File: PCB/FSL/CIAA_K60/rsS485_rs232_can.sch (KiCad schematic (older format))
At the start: 50 parts, among them J401 RS485, J402 DB9, J403 CAN, U401 MAX3072, U402 ST3232E, U403 TJA1040

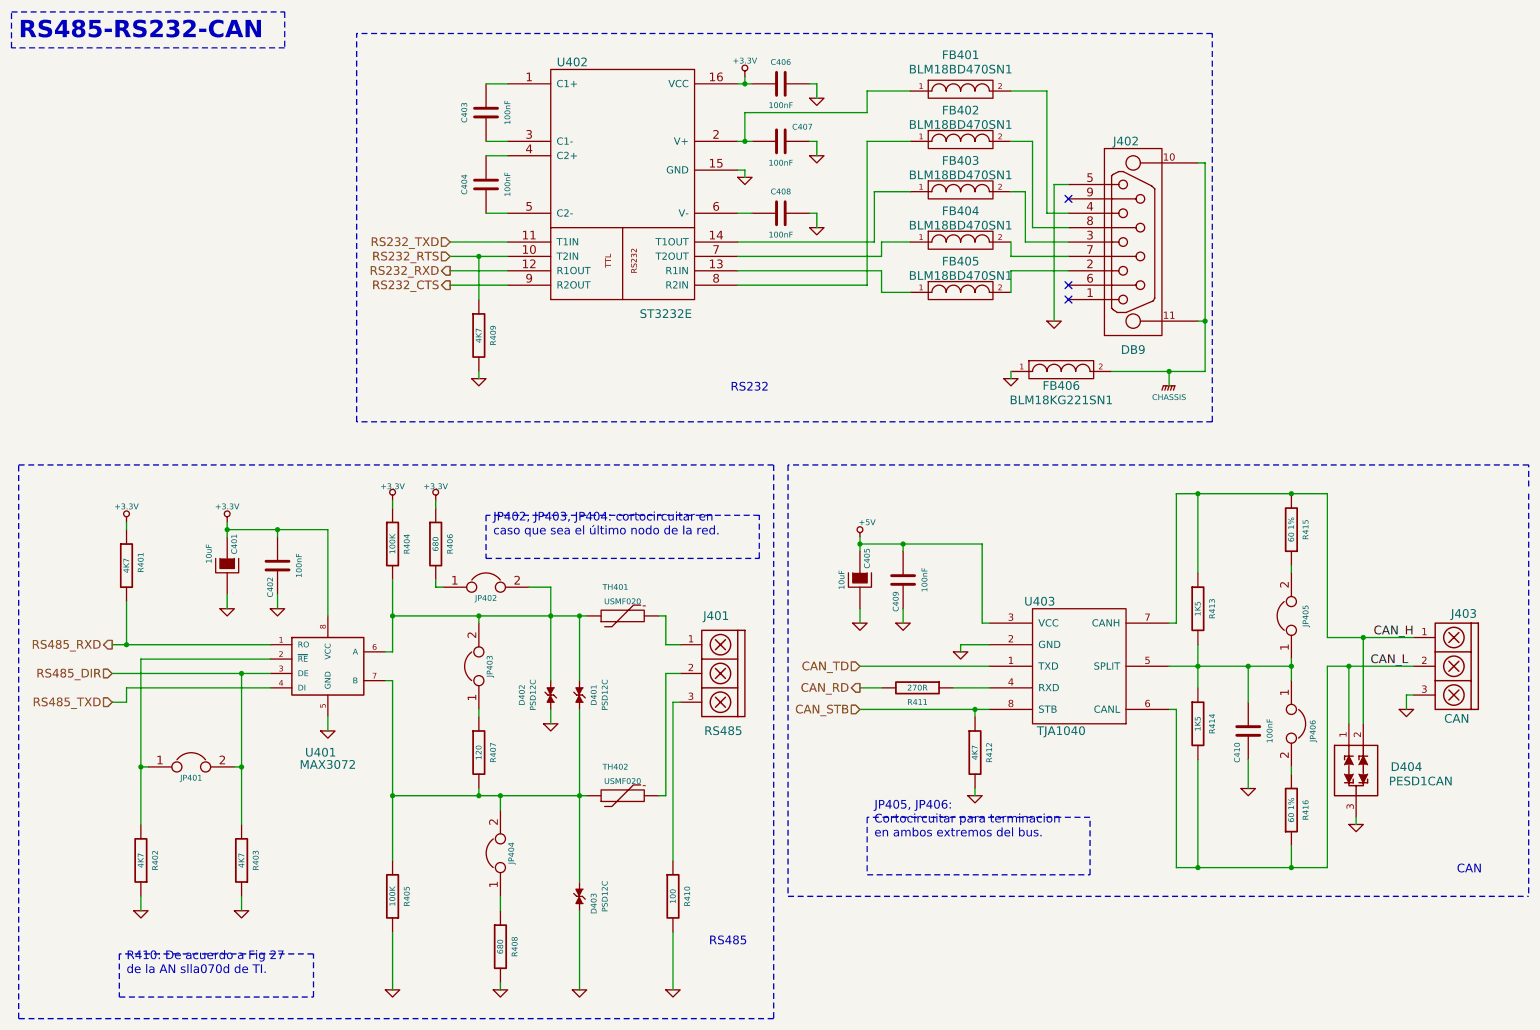
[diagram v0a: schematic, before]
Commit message: Actualizacion de esquematicos. Circuito impreso y modelos 3D
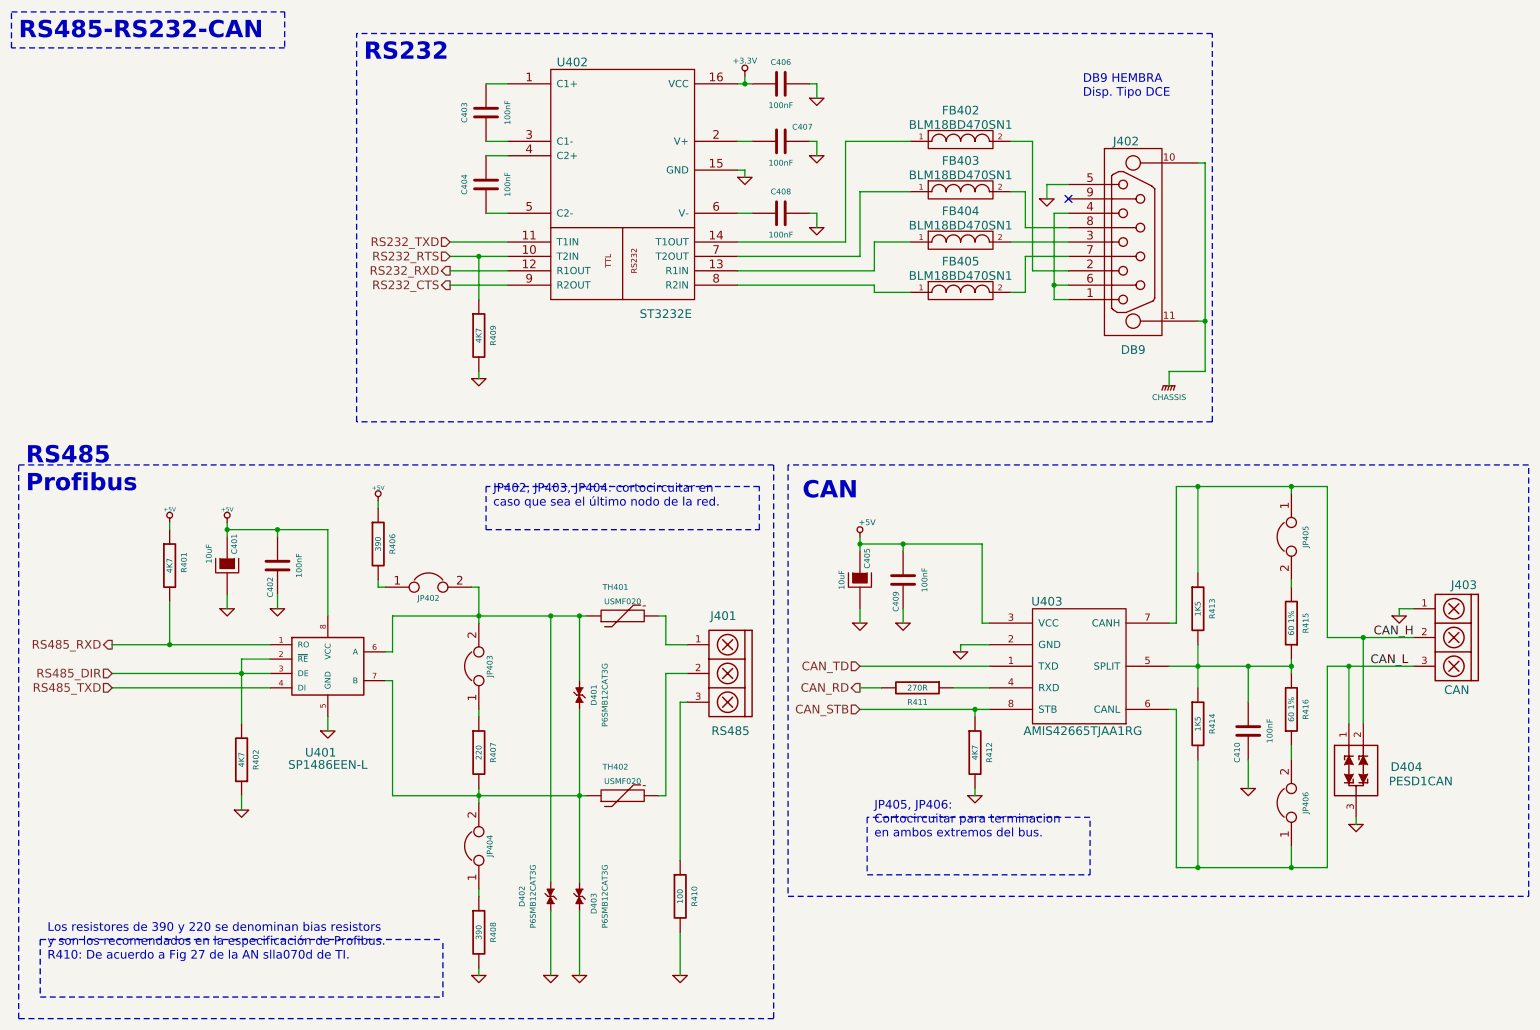
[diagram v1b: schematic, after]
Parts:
- removed FB401: BLM18BD470SN1, fb_0603, symbol FILTER
- removed FB406: BLM18KG221SN1, fb_0603, symbol FILTER
- removed JP401: JUMPER, PIN_ARRAY_2x1, symbol JUMPER
- removed R403: 4K7, r_0603, symbol R
- removed R404, R405: 100K, r_0603, symbol R
- D401, D402, D403: value PSD12C -> P6SMB12CAT3G
- J402: footprint DB9FC -> DB9_F_TH; Descripcion CONN DB9 FEMALE R/A SOLDER SMD -> CONN D-SUB RCPT 9POS RA GOLD; Digikey/Mouser 190-09FA-ND -> S9554-ND; Fabricante Norcomp Inc. -> Sullins; Footprint estandar (none) -> DB9F 7.2mm; Nro. parte 190-009-263R001 -> SDS107-PRP1-F09-SN63-11; Path datasheet ../datasheet/connectors/190-009-263R001.pdf -> ../datasheets/connectors/SDS107-PRP1-F09-SN63-11.pdf
- R406, R408: value 680 -> 390; Descripcion RES 680 OHM 1/10W 5% 0603 SMD -> RES 390 OHM 1/10W 5% 0603 SMD; Digikey/Mouser 311-680GRCT-ND -> 311-390GRCT-ND; Nro. parte RC0603JR-07680RL -> RC0603JR-07390RL
- R407: value 120 -> 220; Descripcion RES 120 OHM 1/10W 5% 0603 SMD -> RES 220 OHM 1/10W 5% 0603 SMD; Digikey/Mouser 311-120GRCT-ND -> 311-220GRCT-ND; Nro. parte RC0603JR-07120RL -> RC0603JR-07220RL
- U401: value MAX3072 -> SP1486EEN-L; Descripcion IC TXRX RS485/422 8-SOIC -> IC TXRX RS485/422 PROFIBUS 8SOIC; Digikey/Mouser MAX3072EESA+-ND -> 1016-1003-5-ND; Fabricante Maxim Integrated -> Exar Corporation; Footprint estandar 8-SOIC (0.154\", 3.90mm Width) -> SOIC-8; Nro. parte MAX3072EESA+ -> SP1486EEN-L; Path datasheet ../datasheet/ic/MAX3070E-MAX3079E.pdf -> ../datasheets/ic/SP1486EEN-L.pdf
- U403: value TJA1040 -> AMIS42665TJAA1RG; Path datasheet ../datasheet/ic/tja1040.pdf -> ../datasheets/ic/AMIS-42665-D.PDF
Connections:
- net +3.3V: no longer C401.1, C402.2, R401.1, R406.1, U401.8 (VCC)
- net +5V: now also C401.1, C402.2, R401.1, R406.1, U401.8 (VCC)
- net CAN_H: now also J403.2, JP405.1; no longer J403.1, R415.2
- net CAN_L: now also J403.3, JP406.1; no longer J403.2, R416.1
- net GND: now also J403.1; no longer J403.3
- net RS485_DIR: now also R402.2, U401.2 (~RE~)
- net at J402.1 (Data_Carrier_Detect): now also J402.4 (DTR), J402.6 (DSR)
- net at J402.2 (Receive_Data): now also FB402.2; no longer FB405.2
- net at J402.3 (Transmit_Data): now also FB404.2; no longer FB403.2
- net at J402.7 (RTS): now also FB405.2; no longer FB404.2
- net at J402.8 (CTS): now also FB403.2; no longer FB402.2
- net at C410.1, R413.2, R414.1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: now also R415.1, R416.2; no longer JP405.1, JP406.1
- net at JP405.2: now also R415.2; no longer R415.1
- net at JP406.2: now also R416.1; no longer R416.2
- net at U402.13 (R1IN): now also FB404.1; no longer FB405.1
- net at U402.14 (T1OUT): now also FB402.1; no longer FB403.1
- net at U402.7 (T2OUT): now also FB403.1; no longer FB404.1
- net at U402.8 (R2IN): now also FB405.1; no longer FB402.1
- no-connect marks 3 -> 1
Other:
- note added: "DB9 HEMBRA\nDisp. Tipo DCE"
- note added: "Los resistores de 390 y 220 se denominan bias resistors\ny son los recomendados en la especificación de Profibus.\nR410: De acuerdo a Fig 27 de la AN slla070d de TI."
- note added: "RS485\nProfibus"
- note removed: "R410: De acuerdo a Fig 27 \nde la AN slla070d de TI.\n"
- note removed: "RS485"
- moved on the sheet: D402, J401, J403, JP402, JP404, JP405, JP406, R401, R402, R406, R410, R415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

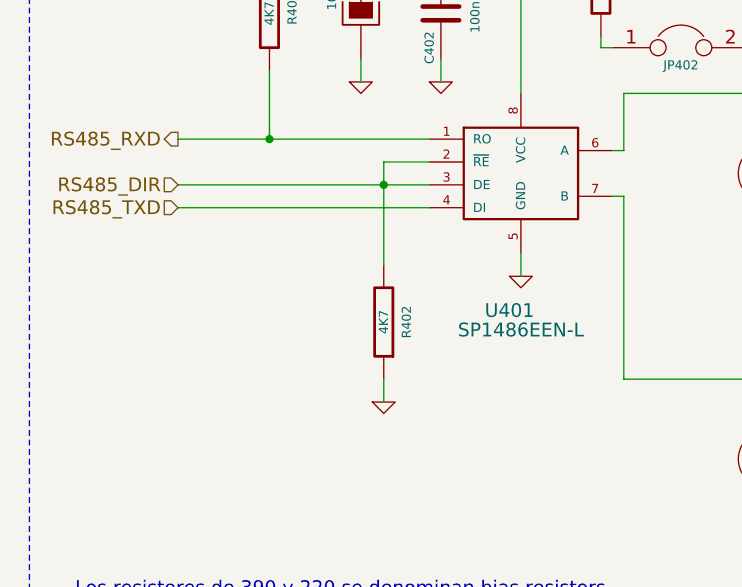
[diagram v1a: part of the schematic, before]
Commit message: - Actualizado PCB - Actualizado documentación - Agregado scripts complementarios de kicad.
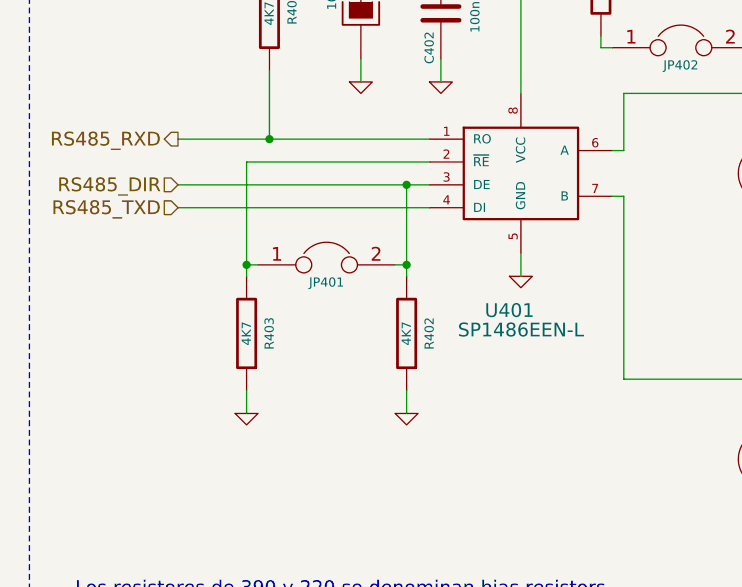
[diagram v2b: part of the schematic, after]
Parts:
- added JP401: JUMPER, PIN_ARRAY_2x1, symbol JUMPER
- added R403: 4K7, r_0603, symbol R
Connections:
- net GND: now also R403.1
- net RS485_DIR: now also JP401.2; no longer U401.2 (~RE~)
- new net: JP401.1, R403.2, U401.2 (~RE~)
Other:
- moved on the sheet: R402

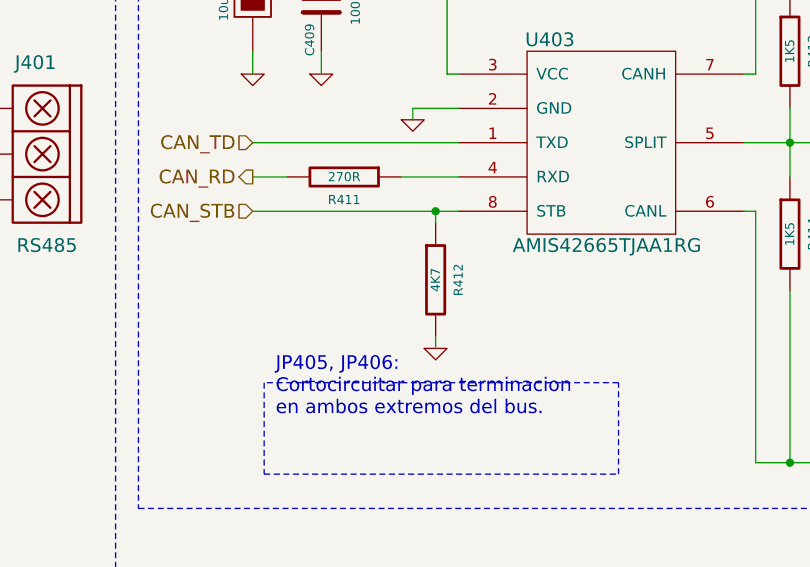
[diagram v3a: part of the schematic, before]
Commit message: CIAA-FSL Versión CEIBO 1.1 - Resumen de cambios en FSL/CIAA_K60/doc/modificaciones - Agregado info de puesta en marcha CEIBO 1.0 - Agregado info de fabricación de la CEIBO 1.0
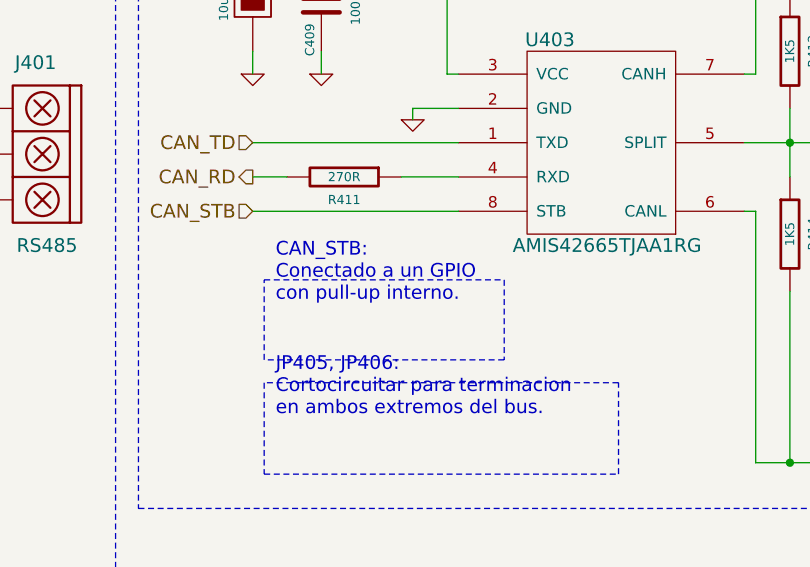
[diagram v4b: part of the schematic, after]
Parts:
- removed R412: 4K7, r_0603, symbol R
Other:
- note added: "CAN_STB:\nConectado a un GPIO\ncon pull-up interno."
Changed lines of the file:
@@
 Sheet 4 13
 Title "CIAA RS485 - RS232 - CAN"
-Date "15 sep 2014"
-Rev "CEIBO 1.0"
+Date "2 dec 2014"
+Rev "CEIBO 1.1"
 Comp "CIAA - COMPUTADORA INDUSTRIAL ABIERTA ARGENTINA. Versión FSL (Freescale K60)"
 Comment1 "Autores: Ver 'doc/CHANGES.txt'      Licencia: Ver  'doc/LICENCIA_CIAA_FSL.txt'"
@@
 $EndComp
 $Comp
-L GND #PWR404
+L GND #PWR059
 U 1 1 52C5B34B
 P 2050 4700
-F 0 "#PWR404" H 2050 4700 30  0001 C CNN
+F 0 "#PWR059" H 2050 4700 30  0001 C CNN
 F 1 "GND" H 2050 4630 30  0001 C CNN
 F 2 "~" H 2050 4700 60  0001 C CNN
@@
 $EndComp
 $Comp
-L GND #PWR417
+L GND #PWR060
 U 1 1 52C5B356
 P 6150 1550
-F 0 "#PWR417" H 6150 1550 30  0001 C CNN
+F 0 "#PWR060" H 6150 1550 30  0001 C CNN
 F 1 "GND" H 6150 1480 30  0001 C CNN
 F 2 "~" H 6150 1550 60  0001 C CNN
@@
 $EndComp
 $Comp
-L GND #PWR418
+L GND #PWR061
 U 1 1 52C5B357
 P 6150 2050
-F 0 "#PWR418" H 6150 2050 30  0001 C CNN
+F 0 "#PWR061" H 6150 2050 30  0001 C CNN
 F 1 "GND" H 6150 1980 30  0001 C CNN
 F 2 "~" H 6150 2050 60  0001 C CNN
@@
 RS485\nProfibus
 $Comp
-L R R412
-U 1 1 52C5B36A
-P 7250 5700
-F 0 "R412" V 7350 5700 40  0000 C CNN
-F 1 "4K7" V 7250 5700 40  0000 C CNN
-F 2 "r_0603" H 7250 5700 60  0001 C CNN
-F 3 "~" H 7250 5700 60  0000 C CNN
-F 4 "RES 4.7K OHM 1/10W 5% 0603 SMD" H 3300 3250 60  0001 C CNN "Descripcion"
-F 5 "Yageo" H 3300 3250 60  0001 C CNN "Fabricante"
-F 6 "RC0603JR-074K7L" H 3300 3250 60  0001 C CNN "Nro. parte"
-F 7 "../datasheet/passive/" H 7250 5700 60  0001 C CNN "Path datasheet"
-F 8 "311-4.7KGRCT-ND" H 3300 3250 60  0001 C CNN "Digikey/Mouser"
-F 9 "0603 (1608 Metric)" H 3300 3250 60  0001 C CNN "Footprint estandar"
-	1    7250 5700
-	1    0    0    -1
-$EndComp
-$Comp
 L TJA1040 U403
 U 1 1 52C5B36B
@@
 $EndComp
 $Comp
-L GND #PWR423
-U 1 1 52C5B36C
-P 7250 6000
-F 0 "#PWR423" H 7250 6000 30  0001 C CNN
-F 1 "GND" H 7250 5930 30  0001 C CNN
-F 2 "~" H 7250 6000 60  0001 C CNN
-F 3 "~" H 7250 6000 60  0001 C CNN
-	1    7250 6000
-	1    0    0    -1
-$EndComp
-$Comp
-L GND #PWR420
+L GND #PWR063
 U 1 1 52C5B36D
 P 6450 4800
-F 0 "#PWR420" H 6450 4800 30  0001 C CNN
+F 0 "#PWR063" H 6450 4800 30  0001 C CNN
 F 1 "GND" H 6450 4730 30  0001 C CNN
 F 2 "~" H 6450 4800 60  0001 C CNN
@@
 $EndComp
 $Comp
-L GND #PWR427
+L GND #PWR064
 U 1 1 52C5B374
 P 9900 6200
-F 0 "#PWR427" H 9900 6200 30  0001 C CNN
+F 0 "#PWR064" H 9900 6200 30  0001 C CNN
 F 1 "GND" H 9900 6130 30  0001 C CNN
 F 2 "~" H 9900 6200 60  0001 C CNN
@@
 $EndComp
 $Comp
-L GND #PWR428
+L GND #PWR065
 U 1 1 52C5B376
 P 10200 4750
-F 0 "#PWR428" H 10200 4750 30  0001 C CNN
+F 0 "#PWR065" H 10200 4750 30  0001 C CNN
 F 1 "GND" H 10200 4680 30  0001 C CNN
 F 2 "~" H 10200 4750 60  0001 C CNN
@@
 $EndComp
 $Comp
-L GND #PWR407
+L GND #PWR066
 U 1 1 52C5B386
 P 2750 5550
-F 0 "#PWR407" H 2750 5550 30  0001 C CNN
+F 0 "#PWR066" H 2750 5550 30  0001 C CNN
 F 1 "GND" H 2750 5480 30  0001 C CNN
 F 2 "~" H 2750 5550 60  0001 C CNN
@@
 $EndComp
 $Comp
-L GND #PWR409
+L GND #PWR067
 U 1 1 52C5B38B
 P 3800 3100
-F 0 "#PWR409" H 3800 3100 30  0001 C CNN
+F 0 "#PWR067" H 3800 3100 30  0001 C CNN
 F 1 "GND" H 3800 3030 30  0001 C CNN
 F 2 "~" H 3800 3100 60  0001 C CNN
@@
 $EndComp
 $Comp
-L GND #PWR415
+L GND #PWR068
 U 1 1 52C620B8
 P 5650 1700
-F 0 "#PWR415" H 5650 1700 30  0001 C CNN
+F 0 "#PWR068" H 5650 1700 30  0001 C CNN
 F 1 "GND" H 5650 1630 30  0001 C CNN
 F 2 "~" H 5650 1700 60  0001 C CNN
@@
 $EndComp
 $Comp
-L GND #PWR416
+L GND #PWR069
 U 1 1 52C622EC
 P 6150 1150
-F 0 "#PWR416" H 6150 1150 30  0001 C CNN
+F 0 "#PWR069" H 6150 1150 30  0001 C CNN
 F 1 "GND" H 6150 1080 30  0001 C CNN
 F 2 "~" H 6150 1150 60  0001 C CNN
@@
 $EndComp
 $Comp
-L +5V #PWR419
+L +5V #PWR070
 U 1 1 52C85C42
 P 6450 4200
-F 0 "#PWR419" H 6450 4290 40  0001 C CNN
+F 0 "#PWR070" H 6450 4290 40  0001 C CNN
 F 1 "+5V" H 6500 4300 40  0000 C CNN
 F 2 "~" H 6450 4200 60  0001 C CNN
@@
 $EndComp
 $Comp
-L +3.3V #PWR414
+L +3.3V #PWR071
 U 1 1 52E1F170
 P 5650 1000
-F 0 "#PWR414" H 5650 960 40  0001 C CNN
+F 0 "#PWR071" H 5650 960 40  0001 C CNN
 F 1 "+3.3V" H 5650 1110 40  0000 C CNN
 F 2 "~" H 5650 1000 60  0001 C CNN
@@
 $EndComp
 $Comp
-L GND #PWR413
+L GND #PWR072
 U 1 1 53925932
 P 5200 7250
-F 0 "#PWR413" H 5200 7250 30  0001 C CNN
+F 0 "#PWR072" H 5200 7250 30  0001 C CNN
 F 1 "GND" H 5200 7180 30  0001 C CNN
 F 2 "~" H 5200 7250 60  0001 C CNN
@@
 RS485-RS232-CAN
 $Comp
-L GND #PWR411
+L GND #PWR073
 U 1 1 539A30FC
 P 4300 7250
-F 0 "#PWR411" H 4300 7250 30  0001 C CNN
+F 0 "#PWR073" H 4300 7250 30  0001 C CNN
 F 1 "GND" H 4300 7180 30  0001 C CNN
 F 2 "~" H 4300 7250 60  0000 C CNN
@@
 $EndComp
 $Comp
-L GND #PWR412
+L GND #PWR074
 U 1 1 539A3255
 P 4500 7250
-F 0 "#PWR412" H 4500 7250 30  0001 C CNN
+F 0 "#PWR074" H 4500 7250 30  0001 C CNN
 F 1 "GND" H 4500 7180 30  0001 C CNN
 F 2 "~" H 4500 7250 60  0000 C CNN
@@
 $EndComp
 $Comp
-L GND #PWR410
+L GND #PWR075
 U 1 1 539A3376
 P 3800 7250
-F 0 "#PWR410" H 3800 7250 30  0001 C CNN
+F 0 "#PWR075" H 3800 7250 30  0001 C CNN
 F 1 "GND" H 3800 7180 30  0001 C CNN
 F 2 "~" H 3800 7250 60  0000 C CNN
@@
 $EndComp
 $Comp
-L GND #PWR405
+L GND #PWR076
 U 1 1 539A3F78
 P 2250 6150
-F 0 "#PWR405" H 2250 6150 30  0001 C CNN
+F 0 "#PWR076" H 2250 6150 30  0001 C CNN
 F 1 "GND" H 2250 6080 30  0001 C CNN
 F 2 "~" H 2250 6150 60  0000 C CNN
@@
 $EndComp
 $Comp
-L GND #PWR406
+L GND #PWR077
 U 1 1 539A44A6
 P 2400 4700
-F 0 "#PWR406" H 2400 4700 30  0001 C CNN
+F 0 "#PWR077" H 2400 4700 30  0001 C CNN
 F 1 "GND" H 2400 4630 30  0001 C CNN
 F 2 "~" H 2400 4700 60  0000 C CNN
@@
 $EndComp
 $Comp
-L GND #PWR421
+L GND #PWR078
 U 1 1 539A4A09
 P 6750 4800
-F 0 "#PWR421" H 6750 4800 30  0001 C CNN
+F 0 "#PWR078" H 6750 4800 30  0001 C CNN
 F 1 "GND" H 6750 4730 30  0001 C CNN
 F 2 "~" H 6750 4800 60  0000 C CNN
@@
 $EndComp
 $Comp
-L GND #PWR422
+L GND #PWR079
 U 1 1 539A4A18
 P 7150 5000
-F 0 "#PWR422" H 7150 5000 30  0001 C CNN
+F 0 "#PWR079" H 7150 5000 30  0001 C CNN
 F 1 "GND" H 7150 4930 30  0001 C CNN
 F 2 "~" H 7150 5000 60  0000 C CNN
@@
 $EndComp
 $Comp
-L GND #PWR426
+L GND #PWR080
 U 1 1 52C5B37A
 P 9150 5950
-F 0 "#PWR426" H 9150 5950 30  0001 C CNN
+F 0 "#PWR080" H 9150 5950 30  0001 C CNN
 F 1 "GND" H 9150 5880 30  0001 C CNN
 F 2 "~" H 9150 5950 60  0001 C CNN
@@
 $EndComp
 $Comp
-L GND #PWR424
+L GND #PWR081
 U 1 1 53A20B62
 P 7750 1850
-F 0 "#PWR424" H 7750 1850 30  0001 C CNN
+F 0 "#PWR081" H 7750 1850 30  0001 C CNN
 F 1 "GND" H 7750 1780 30  0001 C CNN
 F 2 "~" H 7750 1850 60  0001 C CNN
@@
 $EndComp
 $Comp
-L CHASSIS #PWR425
+L CHASSIS #PWR082
 U 1 1 53A22B06
 P 8600 3150
-F 0 "#PWR425" H 8600 3200 40  0001 C CNN
+F 0 "#PWR082" H 8600 3200 40  0001 C CNN
 F 1 "CHASSIS" H 8600 3070 40  0000 C CNN
 F 2 "~" H 8600 3150 60  0000 C CNN
@@
 Wire Wire Line
 	9900 6150 9900 6200
-Wire Wire Line
-	7250 5950 7250 6000
-Connection ~ 7250 5400
-Wire Wire Line
-	7250 5450 7250 5400
 Wire Wire Line
 	7300 4800 7350 4800
@@
 Los resistores de 390 y 220 se denominan bias resistors\ny son los recomendados en la especificación de Profibus.\nR410: De acuerdo a Fig 27 de la AN slla070d de TI.
 $Comp
-L +5V #PWR402
+L +5V #PWR083
 U 1 1 53C5D00C
 P 1650 4100
-F 0 "#PWR402" H 1650 4190 20  0001 C CNN
+F 0 "#PWR083" H 1650 4190 20  0001 C CNN
 F 1 "+5V" H 1650 4190 30  0000 C CNN
 F 2 "~" H 1650 4100 60  0000 C CNN
@@
 $EndComp
 $Comp
-L +5V #PWR403
+L +5V #PWR084
 U 1 1 53C5D02D
 P 2050 4100
-F 0 "#PWR403" H 2050 4190 20  0001 C CNN
+F 0 "#PWR084" H 2050 4190 20  0001 C CNN
 F 1 "+5V" H 2050 4190 30  0000 C CNN
 F 2 "~" H 2050 4100 60  0000 C CNN
@@
 $EndComp
 $Comp
-L +5V #PWR408
+L +5V #PWR085
 U 1 1 53C5D033
 P 3100 3950
-F 0 "#PWR408" H 3100 4040 20  0001 C CNN
+F 0 "#PWR085" H 3100 4040 20  0001 C CNN
 F 1 "+5V" H 3100 4040 30  0000 C CNN
 F 2 "~" H 3100 3950 60  0000 C CNN
@@
 $EndComp
 $Comp
-L GND #PWR401
+L GND #PWR086
 U 1 1 53F5474C
 P 1550 6150
-F 0 "#PWR401" H 1550 6150 30  0001 C CNN
+F 0 "#PWR086" H 1550 6150 30  0001 C CNN
 F 1 "GND" H 1550 6080 30  0001 C CNN
 F 2 "~" H 1550 6150 60  0000 C CNN
@@
 	1600 5500 1550 5500
 Connection ~ 1550 5500
+Text Notes 6550 5800 0    60   ~ 0
+CAN_STB:\nConectado a un GPIO\ncon pull-up interno.
+Wire Notes Line
+	6500 5700 7550 5700
+Wire Notes Line
+	7550 5700 7550 6050
+Wire Notes Line
+	7550 6050 6500 6050
+Wire Notes Line
+	6500 6050 6500 5700
 $EndSCHEMATC
